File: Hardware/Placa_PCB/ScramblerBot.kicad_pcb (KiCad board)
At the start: 2 copper layers, 71 parts, among them J1 OUT LCD, J2 USB_C_Receptacle_PowerOnly_6P, J3 USB_C_Receptacle_USB2.0_16P, J4 Conn_01x03_Pin, J5 Conn_01x03_Pin, J6 Conn_01x03_Pin, J7 Conn_01x03_Pin, J8 Conn_01x08_Pin, J9 Conn_01x18_Pin, Q1 SS8050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

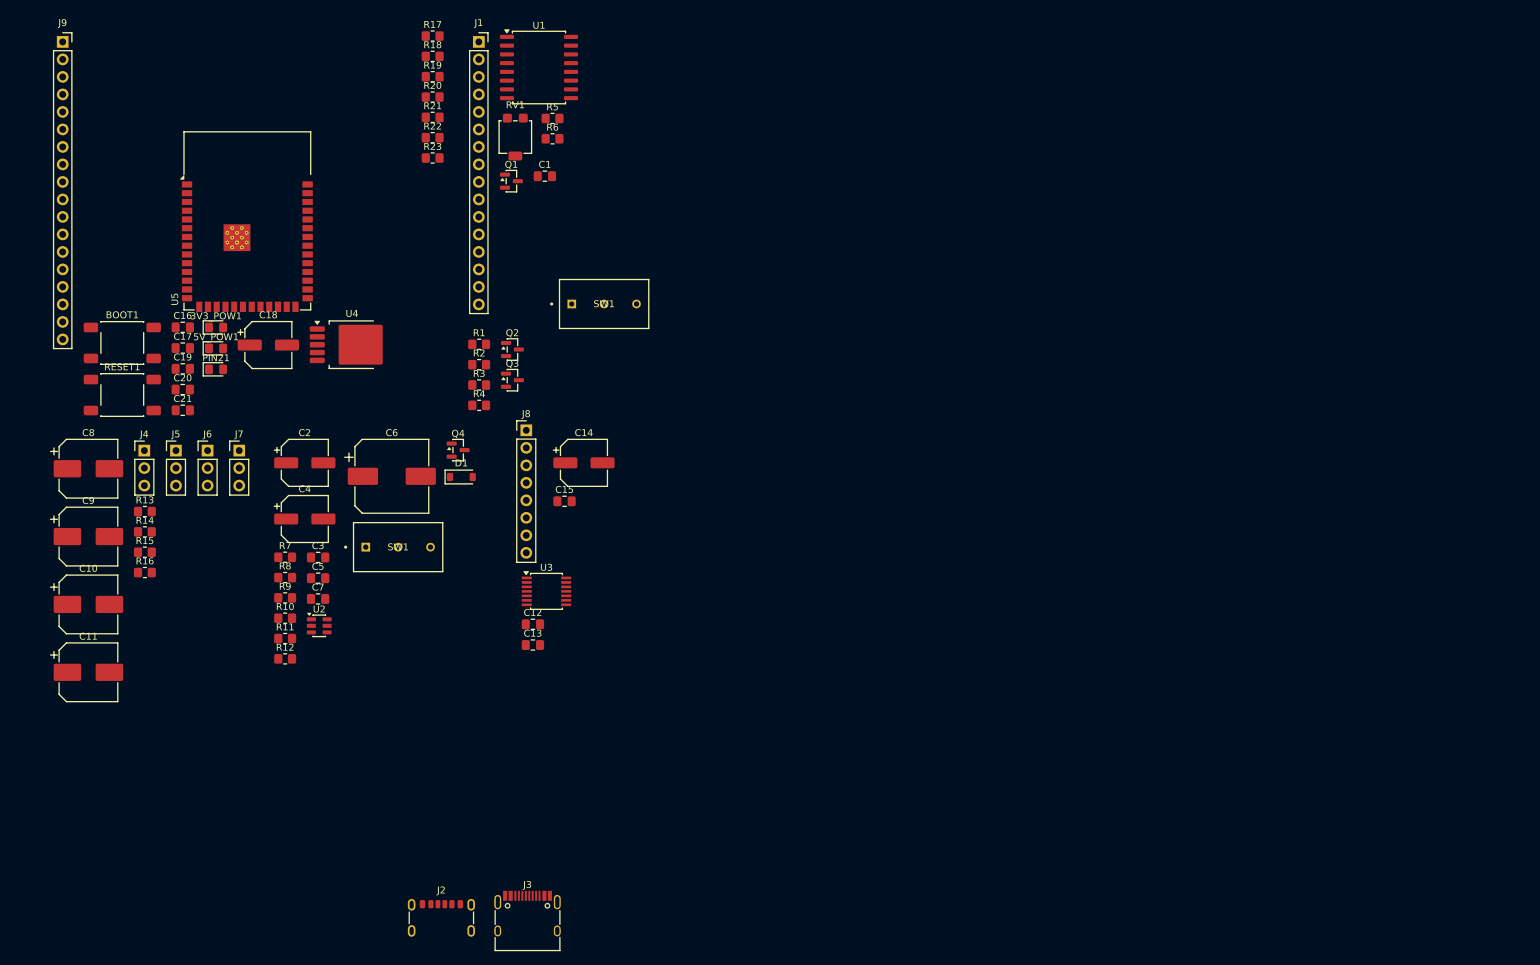
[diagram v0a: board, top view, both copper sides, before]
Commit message: Agregando huella del capacitor de 10uF y comenzando con el PCB (USB + Alimentacion)
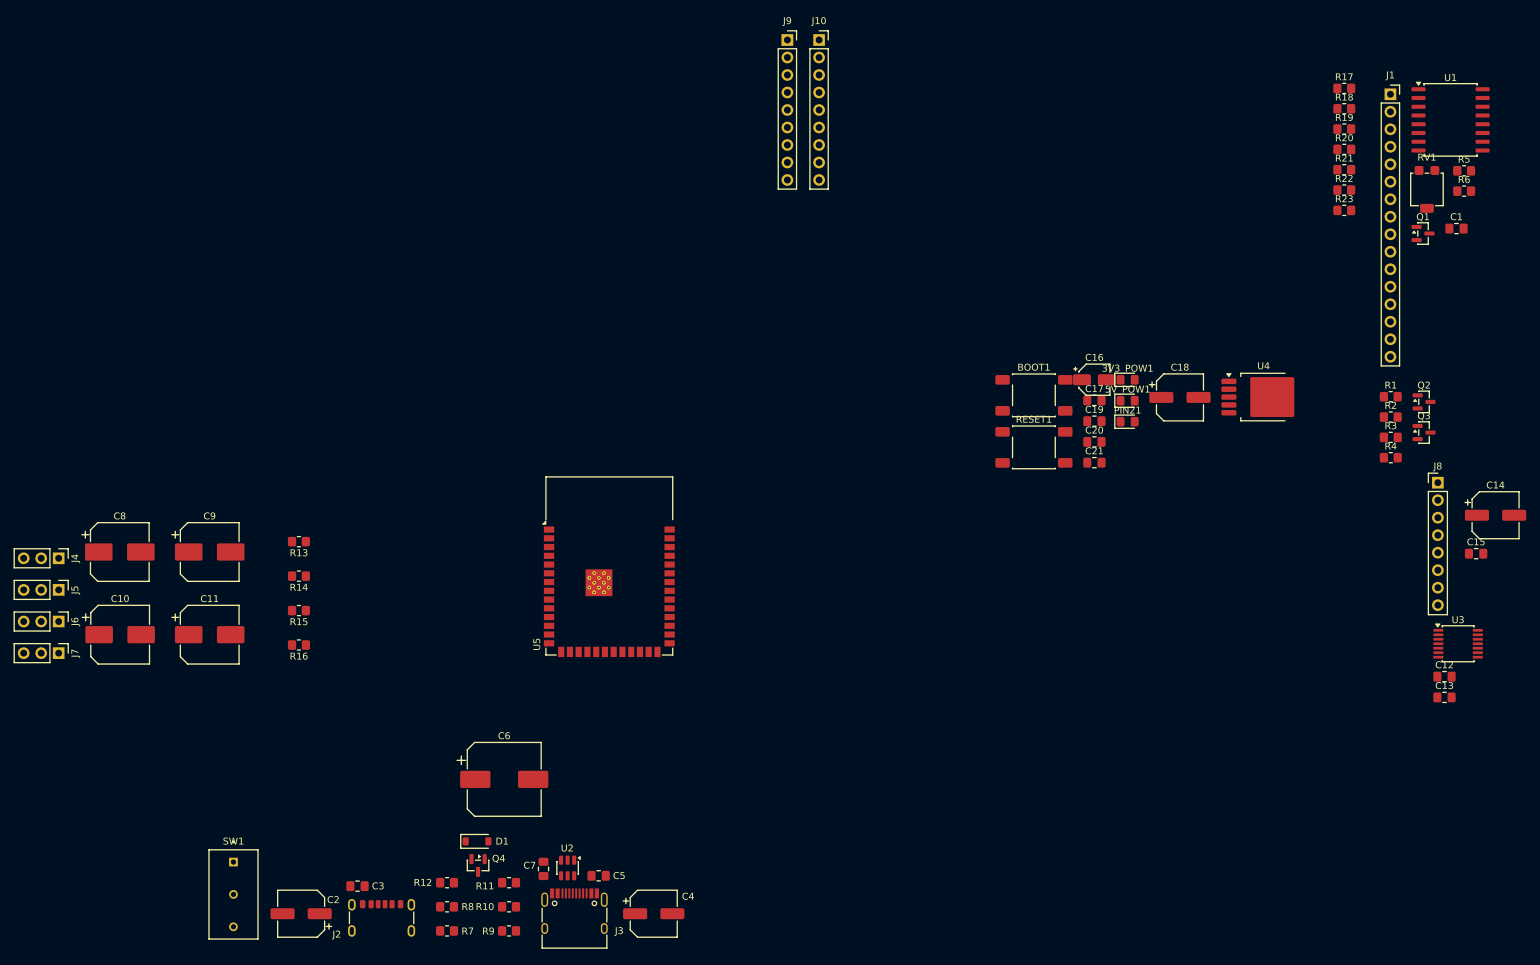
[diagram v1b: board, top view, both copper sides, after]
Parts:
- removed the SW1 at (109.7, 102.8)
- added J10: Conn_01x09_Pin, Connector_PinSocket_2.54mm:PinSocket_1x09_P2.54mm_Vertical, F.Cu at (175.5, 29.2)
- C16: footprint Capacitor_SMD:C_0805_2012Metric_Pad1.18x1.45mm_HandSolder -> Capacitor_SMD:CP_Elec_4x5.4
- J9: value Conn_01x18_Pin -> Conn_01x09_Pin; footprint Connector_PinSocket_2.54mm:PinSocket_1x18_P2.54mm_Vertical -> Connector_PinSocket_2.54mm:PinSocket_1x09_P2.54mm_Vertical
- moved C12 132.5 mm to (266.3, 121.6)
- moved C13 132.5 mm to (266.3, 124.6)
- moved Q1 132.5 mm to (263.2, 57.3)
- moved R1 132.5 mm to (258.5, 81.0)
- moved R2 132.5 mm to (258.5, 83.9)
- moved R3 132.5 mm to (258.5, 86.9)
- moved R4 132.5 mm to (258.5, 89.8)
- moved RV1 132.5 mm to (263.7, 50.9)
- moved U1 132.5 mm to (267.2, 40.8)
- moved 3V3_POW1 132.5 mm to (220.3, 78.5)
- moved 5V_POW1 132.5 mm to (220.3, 81.5)
- moved BOOT1 132.5 mm to (206.7, 80.8)
- moved C1 132.5 mm to (268.0, 56.5)
- moved C14 132.5 mm to (273.7, 98.2)
- moved C15 132.5 mm to (270.9, 103.7)
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
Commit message: Acomodando los componentes en el PCB y cambiendo las conexiones con el ESP32
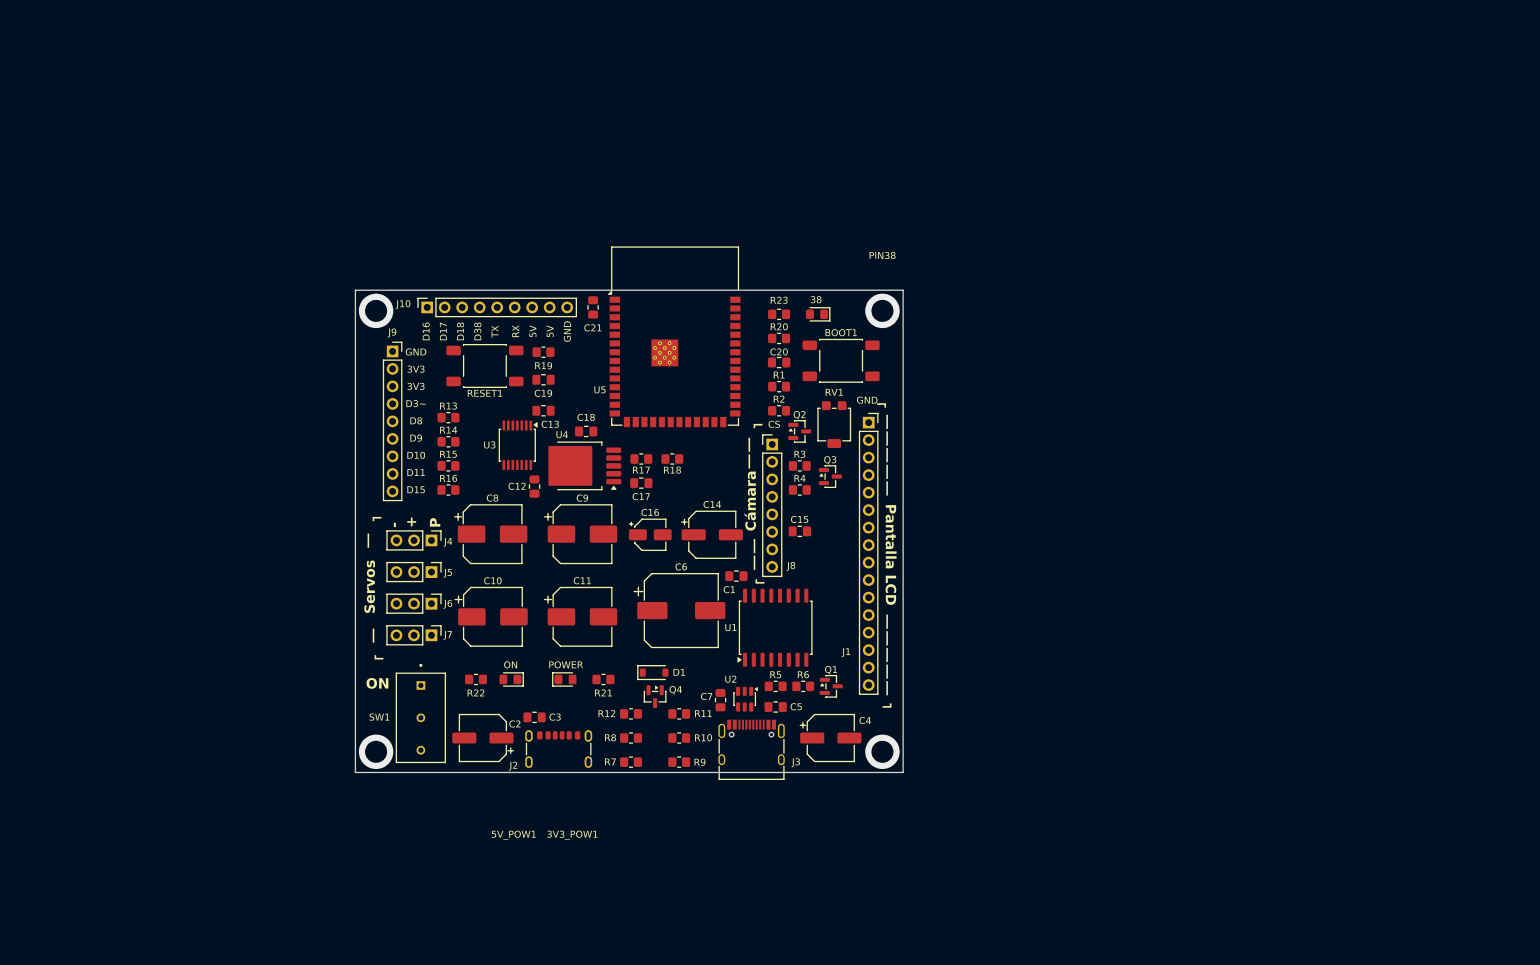
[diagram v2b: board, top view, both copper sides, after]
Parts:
- C18: footprint Capacitor_SMD:CP_Elec_6.3x5.8 -> Capacitor_SMD:C_0805_2012Metric_Pad1.18x1.45mm_HandSolder
- moved R22 144.7 mm to (125.7, 122.0)
- moved U3 139.6 mm to (131.7, 88.0), turned to -90 degrees
- moved C13 137.2 mm to (135.5, 83.0)
- moved C12 134.9 mm to (134.2, 94.0), turned to -90 degrees
- moved R21 130.5 mm to (144.2, 122.0), turned to 180 degrees
- moved R5 124.8 mm to (169.2, 123.0)
- moved U1 122.6 mm to (169.2, 114.5), turned to 90 degrees
- moved R19 120.7 mm to (135.5, 74.5), turned to 180 degrees
- moved R6 119.9 mm to (173.2, 123.0)
- moved C1 116.1 mm to (163.5, 107.0), turned to 180 degrees
- moved R17 115.3 mm to (149.7, 90.0), turned to 180 degrees
- moved C14 113.7 mm to (160.0, 101.0)
- moved R18 110.0 mm to (154.2, 90.0), turned to 180 degrees
- moved Q1 108.2 mm to (177.3, 123.0)
- moved U4 99.9 mm to (140.7, 91.0), turned to 180 degrees
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- renumbered PIN21 to PIN38
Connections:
- U5 pad 20: /Camara/SDA -> /Camara/SCL
- U5 pad 21: /Camara/SCL -> /Camara/SDA
- U5 pad 22: /Camara/MOSI -> /Camara/SCK
- U5 pad 24: /Camara/CS -> /Camara/MOSI
- U5 pad 25: /Camara/SCK -> /Camara/CS
- U5 pad 4: /Level Shifter PWM/PWM1 -> /Level Shifter PWM/PWM4
- U5 pad 5: /Level Shifter PWM/PWM2 -> /Level Shifter PWM/PWM3
- U5 pad 6: /Level Shifter PWM/PWM3 -> /Level Shifter PWM/PWM2
- U5 pad 7: /Level Shifter PWM/PWM4 -> /Level Shifter PWM/PWM1
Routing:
- net GNDD: vias 0 -> 4
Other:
- board outline added: 79.5 x 70 mm
- board text added: "+"
- board text added: "-"
- board text added: "38"
- board text added: "3V3"
- board text added: "5V"
- board text added: "CS"
- board text added: "Cámara"
- board text added: "D10"
- board text added: "D11"
- board text added: "D15"
- board text added: "D16"
- board text added: "D17"
- board text added: "D18"
- board text added: "D38"
- board text added: "D3~"
- board text added: "D8"
- board text added: "D9"
- board text added: "GND"
- board text added: "ON"
- board text added: "P"
- board text added: "POWER"
- board text added: "Pantalla LCD"
- board text added: "RX"
- board text added: "Servos"
- board text added: "TX"
- board text added: "|"
- board text added: "| |"
- board text added: "| | | | |"
- board text added: "¬"
- board text added: "⌐"

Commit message: Terminando el enrutado de los +5V y comenzando las pistas de 3.3V
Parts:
- moved C16 13.1 mm to (161.0, 92.5)
- moved R5 10.3 mm to (178.5, 118.5)
- moved R18 8.76 mm to (149.7, 97.5), turned to 0 degrees
- moved R7 3.50 mm to (148.2, 130.5)
- moved R8 3.50 mm to (148.2, 134.0)
- moved J10 1.82 mm to (116.8, 68.0)
- moved C5 1.28 mm to (170.0, 125.0)
- moved C21 0.86 mm to (142.0, 67.5), turned to 180 degrees
- moved U2 0.78 mm to (165.4, 124.5)
- moved Q1 0.74 mm to (178.0, 123.0)
- moved C12 0.70 mm to (133.5, 94.0), turned to 0 degrees
- moved C18 0.70 mm to (141.0, 86.0)
- moved 3V3_POW1 0.50 mm to (138.7, 121.5)
- moved 5V_POW1 0.50 mm to (130.7, 121.5)
- moved R21 0.50 mm to (144.2, 121.5)
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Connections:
- J10 pad 7: +5V -> +3.3V
- J10 pad 8: +5V -> +3.3V
- J9 pad 2: +3.3V -> +5V
- J9 pad 3: +3.3V -> +5V
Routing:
- net /MCU/USB_D+: track 0.00 -> 59.3 mm
- net +5V: track 0.00 -> 59.2 mm, vias 0 -> 4
- net /MCU/USB_D-: track 0.00 -> 58.5 mm
- net /MCU/LED_USB: track 0.00 -> 47.5 mm
- net /MCU/9: track 0.00 -> 40.7 mm, vias 0 -> 2
- net GNDD: track 0.00 -> 35.7 mm, vias 4 -> 30
- net /Camara/SCL: track 0.00 -> 34.8 mm, vias 0 -> 2
- net /Pantalla_LCD/RS: track 0.00 -> 33.6 mm, vias 0 -> 2
- net /Camara/SDA: track 0.00 -> 32.9 mm, vias 0 -> 2
- net /Level Shifter LCD/SCL_LCD: track 0.00 -> 30.1 mm, vias 0 -> 2
- net /Pantalla_LCD/RW: track 0.00 -> 29.6 mm, vias 0 -> 2
- net /Pantalla_LCD/EN_LCD: track 0.00 -> 28.4 mm, vias 0 -> 2
- net /Level Shifter LCD/SDA_ESP32: track 0.00 -> 28.3 mm, vias 0 -> 2
- net /Level Shifter LCD/SCL_ESP32: track 0.00 -> 25.8 mm, vias 0 -> 4
- net /Level Shifter LCD/SDA_LCD: track 0.00 -> 21.5 mm, vias 0 -> 2
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- added copper zone on B.Cu, net +3.3V
- added copper zone on F.Cu, net +5V
- added copper zone on F.Cu, net /Power__USB_C/V_USB_POWER
- added copper zone on F.Cu, net /Power__USB_C/V_USB_PROG
- added copper zone on In1.Cu, net GNDD
- added copper zone on In2.Cu, net GNDD
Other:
- copper layers 2 -> 4

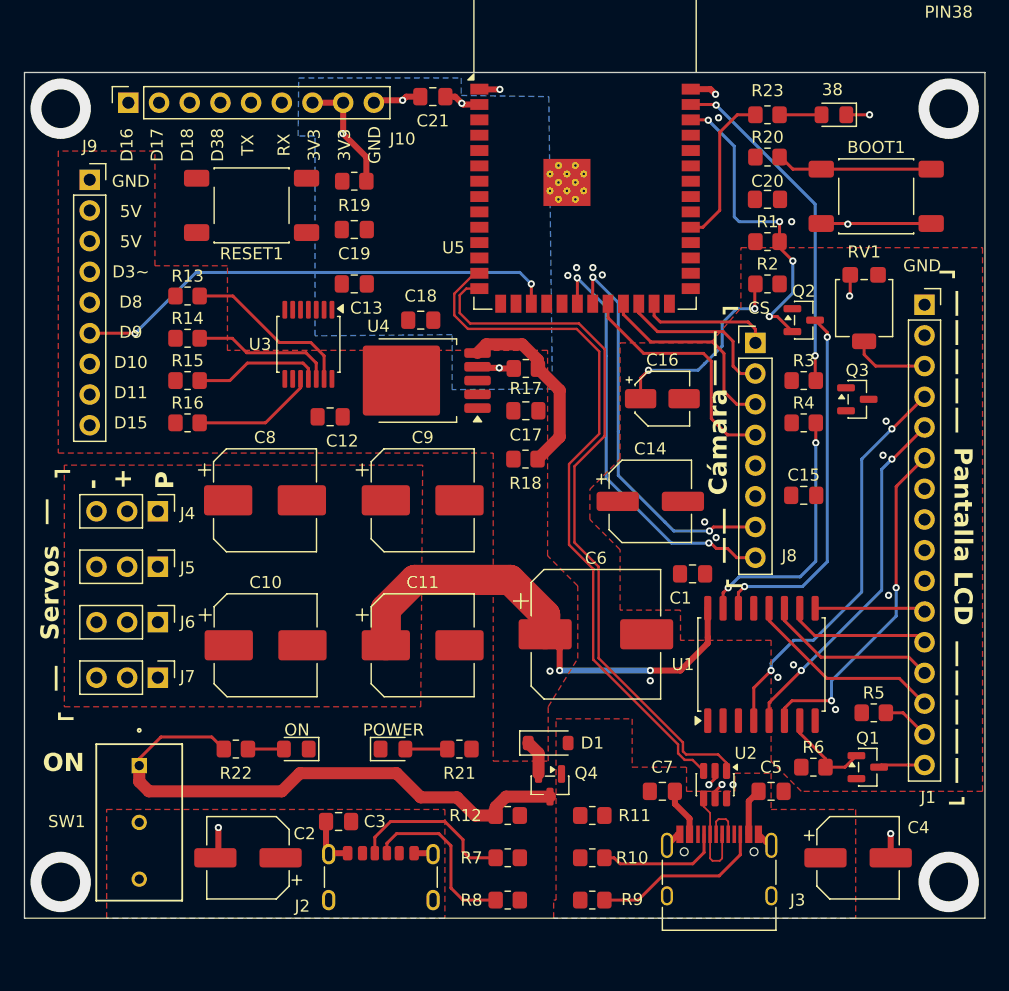
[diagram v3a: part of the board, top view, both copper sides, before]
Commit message: Actualizacion de PCB con rellenos ordenados, solo falta colocar las vias
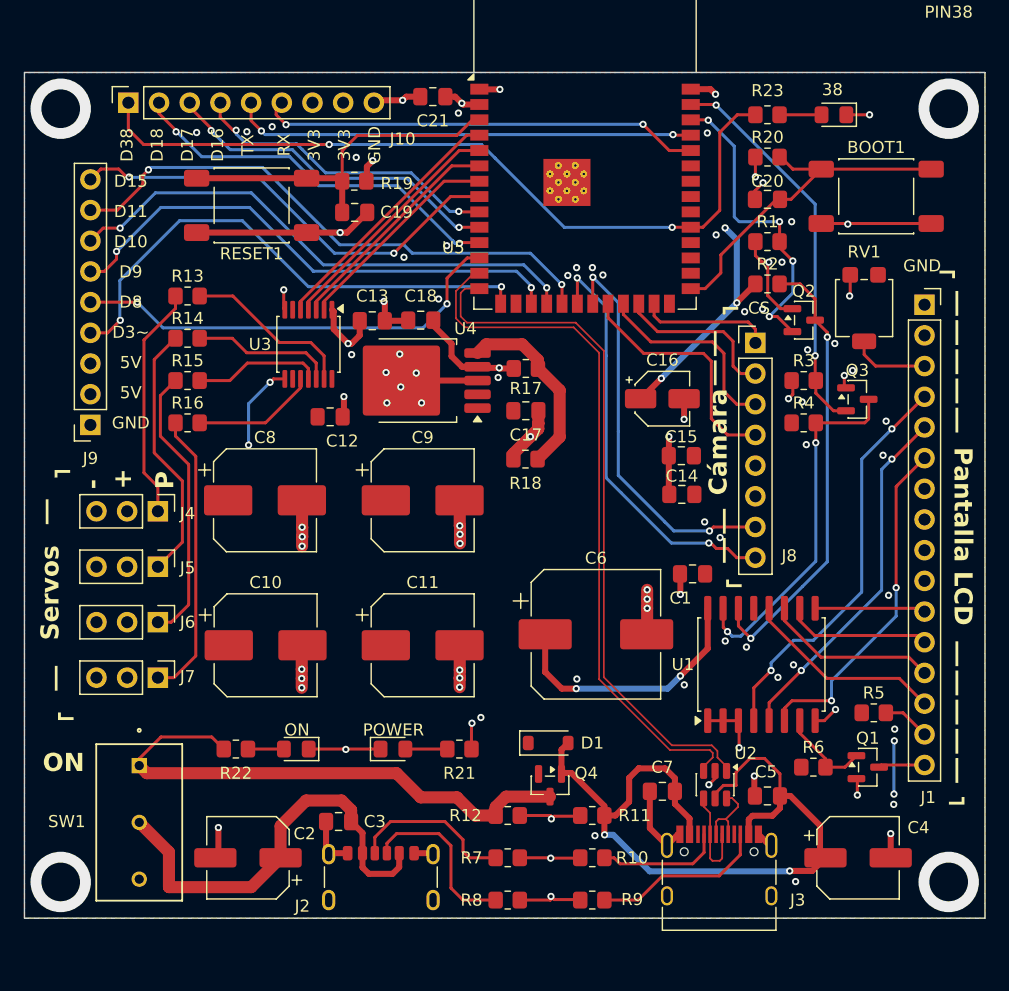
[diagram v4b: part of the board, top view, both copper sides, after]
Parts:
- C14: value 100uF -> 10uF; footprint Capacitor_SMD:CP_Elec_6.3x5.8 -> Capacitor_SMD:C_0805_2012Metric_Pad1.18x1.45mm_HandSolder
- moved J9 20.3 mm to (113.7, 94.7), turned to 180 degrees
- moved C15 10.6 mm to (162.6, 97.2), turned to 180 degrees
- moved C13 3.39 mm to (137.0, 86.0)
- moved C14 2.67 mm to (162.6, 100.4)
- moved C19 1.42 mm to (135.5, 77.1)
- moved C5 0.49 mm to (169.7, 125.4), turned to 180 degrees
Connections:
- C14 pad 1: +5V -> GNDD
- C14 pad 2: GNDD -> +5V
- J10 pad 1: /MCU/16 -> /MCU/38 - LED
- J10 pad 2: /MCU/17 -> /MCU/18
- J10 pad 3: /MCU/18 -> /MCU/17
- J10 pad 4: /MCU/38 - LED -> /MCU/16
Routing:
- net GNDD: track 35.7 -> 134.0 mm, vias 30 -> 92
- net /Power__USB_C/V_USB_PROG: track 9.34 -> 66.4 mm, vias 1 -> 2
- net /MCU/38 - LED: track 13.0 -> 65.1 mm, vias 0 -> 2
- net /MCU/11: track 0.00 -> 46.5 mm, vias 0 -> 2
- net /MCU/10: track 0.00 -> 44.0 mm, vias 0 -> 2
- net /MCU/3: track 0.00 -> 43.5 mm, vias 0 -> 2
- net /MCU/TX: track 0.00 -> 38.4 mm, vias 0 -> 2
- net /MCU/15: track 0.00 -> 37.4 mm, vias 0 -> 2
- net /MCU/RX: track 0.00 -> 36.8 mm, vias 0 -> 2
- net /MCU/8: track 0.00 -> 36.7 mm, vias 0 -> 2
- net /Power__USB_C/V_USB_POWER: track 0.00 -> 36.1 mm
- net /MCU/18: track 0.00 -> 32.0 mm, vias 0 -> 2
- net /MCU/EN: track 0.00 -> 29.7 mm
- net /MCU/17: track 0.00 -> 28.6 mm, vias 0 -> 2
- net /MCU/16: track 0.00 -> 26.1 mm, vias 0 -> 2
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- removed copper zone on F.Cu, net /Power__USB_C/V_USB_POWER
- removed copper zone on F.Cu, net /Power__USB_C/V_USB_PROG

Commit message: PCB Final 1
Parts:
- added G***: LOGO, Images:flecha, F.Cu at (138.0, 132.2)
- added G***: LOGO, Images:flecha, F.Cu at (166.3, 132.0)
- added G***: LOGO, Images_ScramblerBot:logo_ScramblerBot_40x16, F.Cu at (148.8, 79.7)
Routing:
- net +5V: track 53.7 -> 63.5 mm, vias 9 -> 39
- net /Power__USB_C/V_USB_POWER: track 36.1 -> 44.1 mm
- net GNDD: track 134.0 -> 129.6 mm, vias 92 -> 288
- net +3.3V: track 34.4 -> 34.1 mm, vias 9 -> 17
- net /MCU/BOOT: vias 0 -> 2
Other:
- board text added: "+ Esteban Ruiz"
- board text added: "+5V"
- board text added: "5V 3A"
- board text added: "A"
- board text added: "D0"
- board text added: "D1"
- board text added: "D2"
- board text added: "D3"
- board text added: "D4"
- board text added: "D5"
- board text added: "D6"
- board text added: "D7"
- board text added: "EN"
- board text added: "K"
- board text added: "MISO"
- board text added: "MOSI"
- board text added: "OFF"
- board text added: "PROG."
- board text added: "PWM1"
- board text added: "PWM2"
- board text added: "PWM3"
- board text added: "PWM4"
- board text added: "RS"
- board text added: "RW"
- board text added: "SCK"
- board text added: "SCL"
- board text added: "SDA"
- board text added: "V0"
- board text added: "by + Camila Cáceres"
- board text added: "for WCA Competitions"
